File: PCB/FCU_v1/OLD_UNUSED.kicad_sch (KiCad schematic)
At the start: 22 parts, among them J4 Conn_Coaxial_Small, U5 LIS2MDL, U6 LPS22HH, U9 MAX-M10M-20B

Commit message: Schematic update
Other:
- note added: "Previous implementation idea Changed to different parts Left for possible future use Excluded from board"
- moved on the sheet: C10, C23, C24, C25, C26, C27, C28, C29, C32, C35, D4, J4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

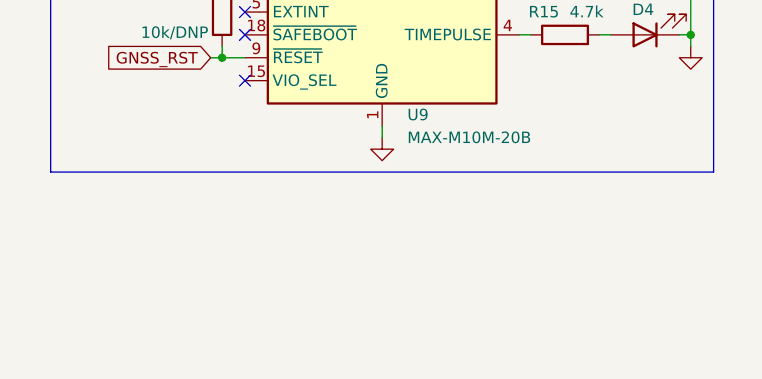
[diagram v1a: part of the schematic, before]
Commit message: Components change and layout update
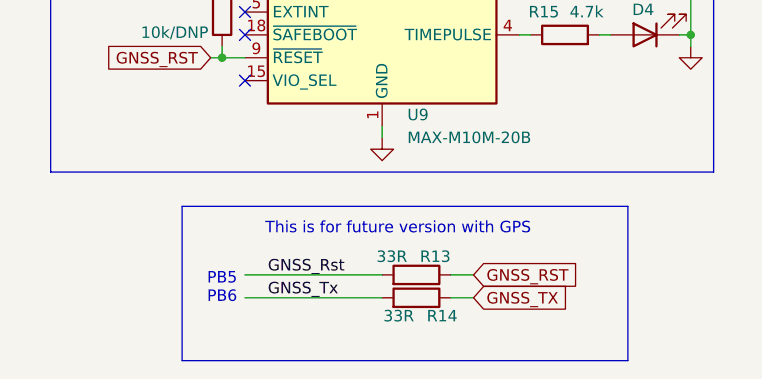
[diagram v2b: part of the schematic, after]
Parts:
- added R13, R14: 33R, Resistor_SMD:R_0603_1608Metric, symbol Device:R
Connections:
- net GNSS_RST: now also R13.1
- net GNSS_TX: now also R14.1
- new net GNSS_Rst: R13.2
- new net GNSS_Tx: R14.2
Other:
- note added: "PB5 PB6"
- note added: "This is for future version with GPS"
